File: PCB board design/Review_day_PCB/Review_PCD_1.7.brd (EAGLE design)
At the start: 55.9 x 54.3 mm, 10 parts, among them Q1 16 MHz, Q2 2N7000, U1 ATMEGA328P_VQFNVQFN

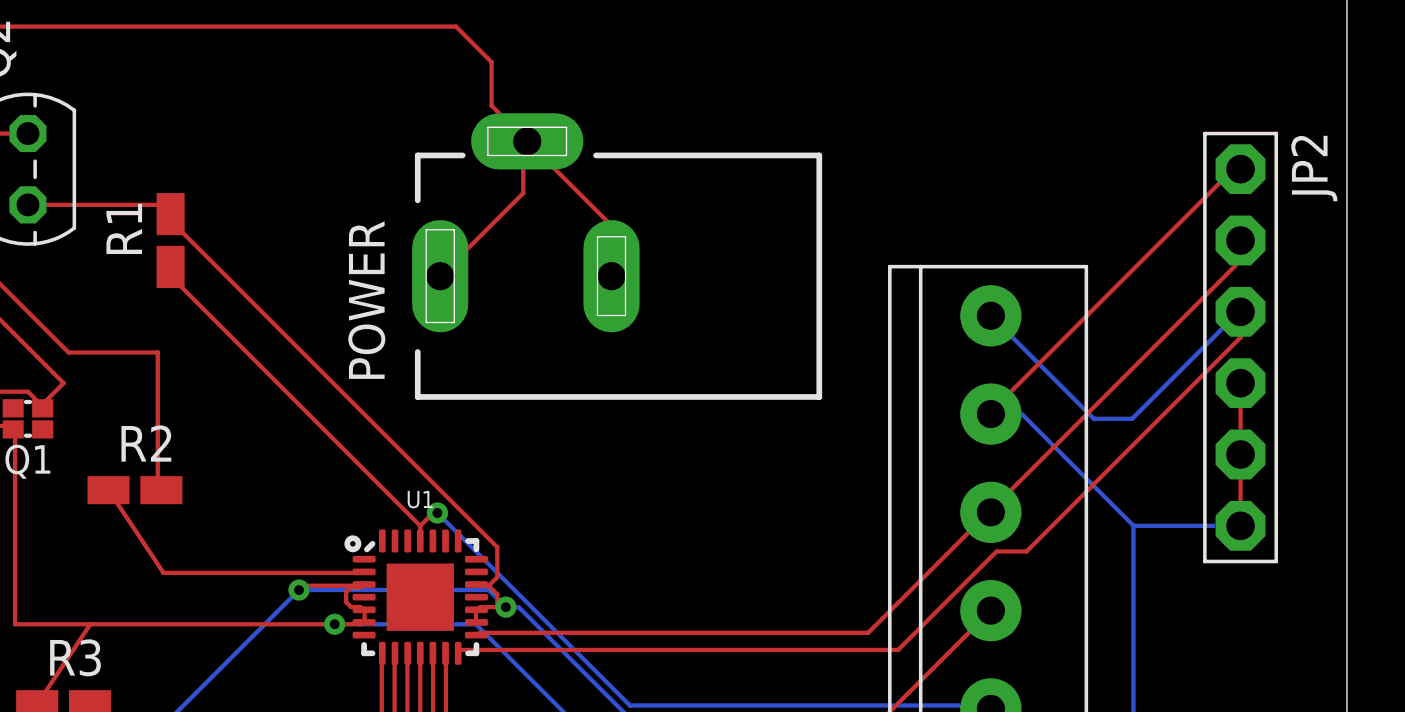
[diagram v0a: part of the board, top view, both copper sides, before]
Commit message: cleared fixable errors
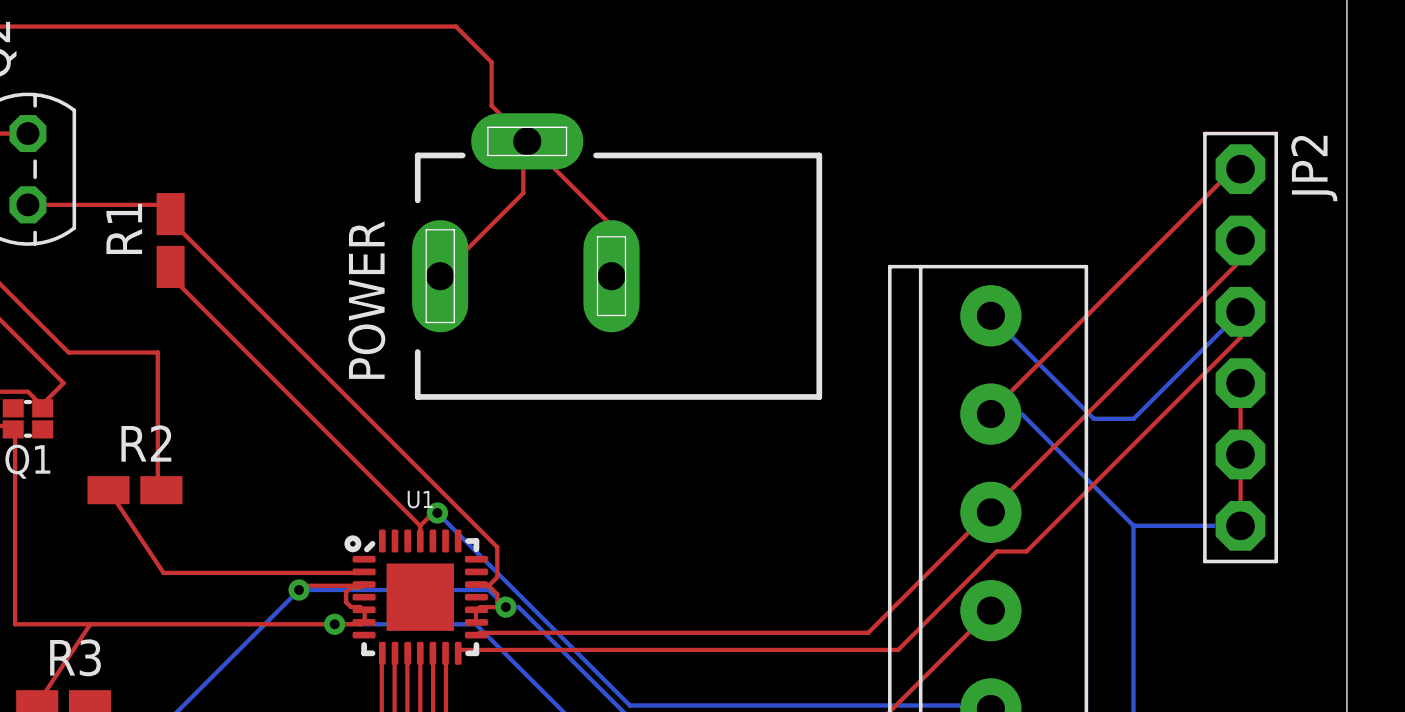
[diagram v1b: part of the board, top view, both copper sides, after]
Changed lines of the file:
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@@
 <wire x1="84.4296" y1="57.6072" x2="91.2876" y2="50.7492" width="0.1524" layer="16"/>
 <wire x1="104.0384" y1="50.7492" x2="104.14" y2="50.63" width="0.1524" layer="16"/>
-<wire x1="83.82" y1="56.6928" x2="83.82" y2="56.61" width="0.1524" layer="1"/>
 <via x="84.4296" y="57.6072" extent="1-16" drill="0.35"/>
-<wire x1="83.82" y1="56.61" x2="83.82" y2="57.15" width="0.1524" layer="1"/>
-<wire x1="83.82" y1="57.15" x2="74.93" y2="66.04" width="0.1524" layer="1"/>
+<wire x1="74.93" y1="66.04" x2="83.82" y2="57.15" width="0.1524" layer="1"/>
 <wire x1="83.82" y1="57.15" x2="84.2772" y2="57.6072" width="0.1524" layer="1"/>
 <wire x1="84.2772" y1="57.6072" x2="84.4296" y2="57.6072" width="0.1524" layer="1"/>
+<wire x1="83.82" y1="57.15" x2="83.82" y2="56.61" width="0.1524" layer="1"/>
 </signal>
 <signal name="N$3">
@@
 <wire x1="104.3432" y1="56.2356" x2="105.41" y2="56.2356" width="0.1524" layer="1"/>
 <wire x1="85.1916" y1="52.7304" x2="85.17" y2="52.61" width="0.1524" layer="1"/>
-<wire x1="109.1692" y1="60.96" x2="107.81" y2="60.96" width="0.1524" layer="16"/>
 <wire x1="104.14" y1="64.63" x2="107.81" y2="60.96" width="0.1524" layer="16"/>
-<wire x1="112.9792" y1="64.77" x2="112.9538" y2="64.7446" width="0.1524" layer="16"/>
-<wire x1="112.9538" y1="64.7446" x2="109.1692" y2="60.96" width="0.1524" layer="16"/>
 <wire x1="105.41" y1="56.2356" x2="113.03" y2="63.8556" width="0.1524" layer="1"/>
 <contactref element="JP2" pad="3"/>
 <wire x1="113.03" y1="64.77" x2="113.03" y2="63.8556" width="0.1524" layer="1"/>
-<wire x1="112.9284" y1="64.77" x2="112.9538" y2="64.7446" width="0.1524" layer="16"/>
-<wire x1="112.9284" y1="64.77" x2="113.03" y2="64.77" width="0.1524" layer="16"/>
+<wire x1="109.22" y1="60.96" x2="113.03" y2="64.77" width="0.1524" layer="16"/>
+<wire x1="107.81" y1="60.96" x2="109.22" y2="60.96" width="0.1524" layer="16"/>
 </signal>
 <signal name="D7">
@@
 </signal>
 <signal name="C">
-<contactref element="Q1" pad="3"/>
-<contactref element="Q1" pad="1"/>
 <contactref element="R3" pad="1"/>
 <contactref element="U1" pad="5"/>
@@
 <wire x1="67.3608" y1="31.8516" x2="67.31" y2="31.75" width="0.1524" layer="16"/>
 <wire x1="112.7252" y1="69.7992" x2="112.9284" y2="69.7992" width="0.1524" layer="1"/>
-<wire x1="112.9284" y1="69.7992" x2="112.9792" y2="69.7992" width="0.1524" layer="1"/>
 <wire x1="104.1908" y1="61.2648" x2="112.7252" y2="69.7992" width="0.1524" layer="1"/>
 <wire x1="104.1908" y1="61.2648" x2="104.14" y2="61.13" width="0.1524" layer="1"/>
@@
 <wire x1="109.22" y1="57.15" x2="113.03" y2="57.15" width="0.1524" layer="16"/>
 <wire x1="112.9284" y1="69.7992" x2="113.03" y2="69.85" width="0.1524" layer="1"/>
+<contactref element="Q1" pad="1"/>
+<contactref element="Q1" pad="3"/>
 </signal>
 <signal name="N$1">
